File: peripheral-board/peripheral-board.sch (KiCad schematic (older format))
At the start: 7 parts, among them CON1001 AVR-ISP-10, IC1001 ATTINY48-A, P1001 Peripheral Bus, P1002 Power

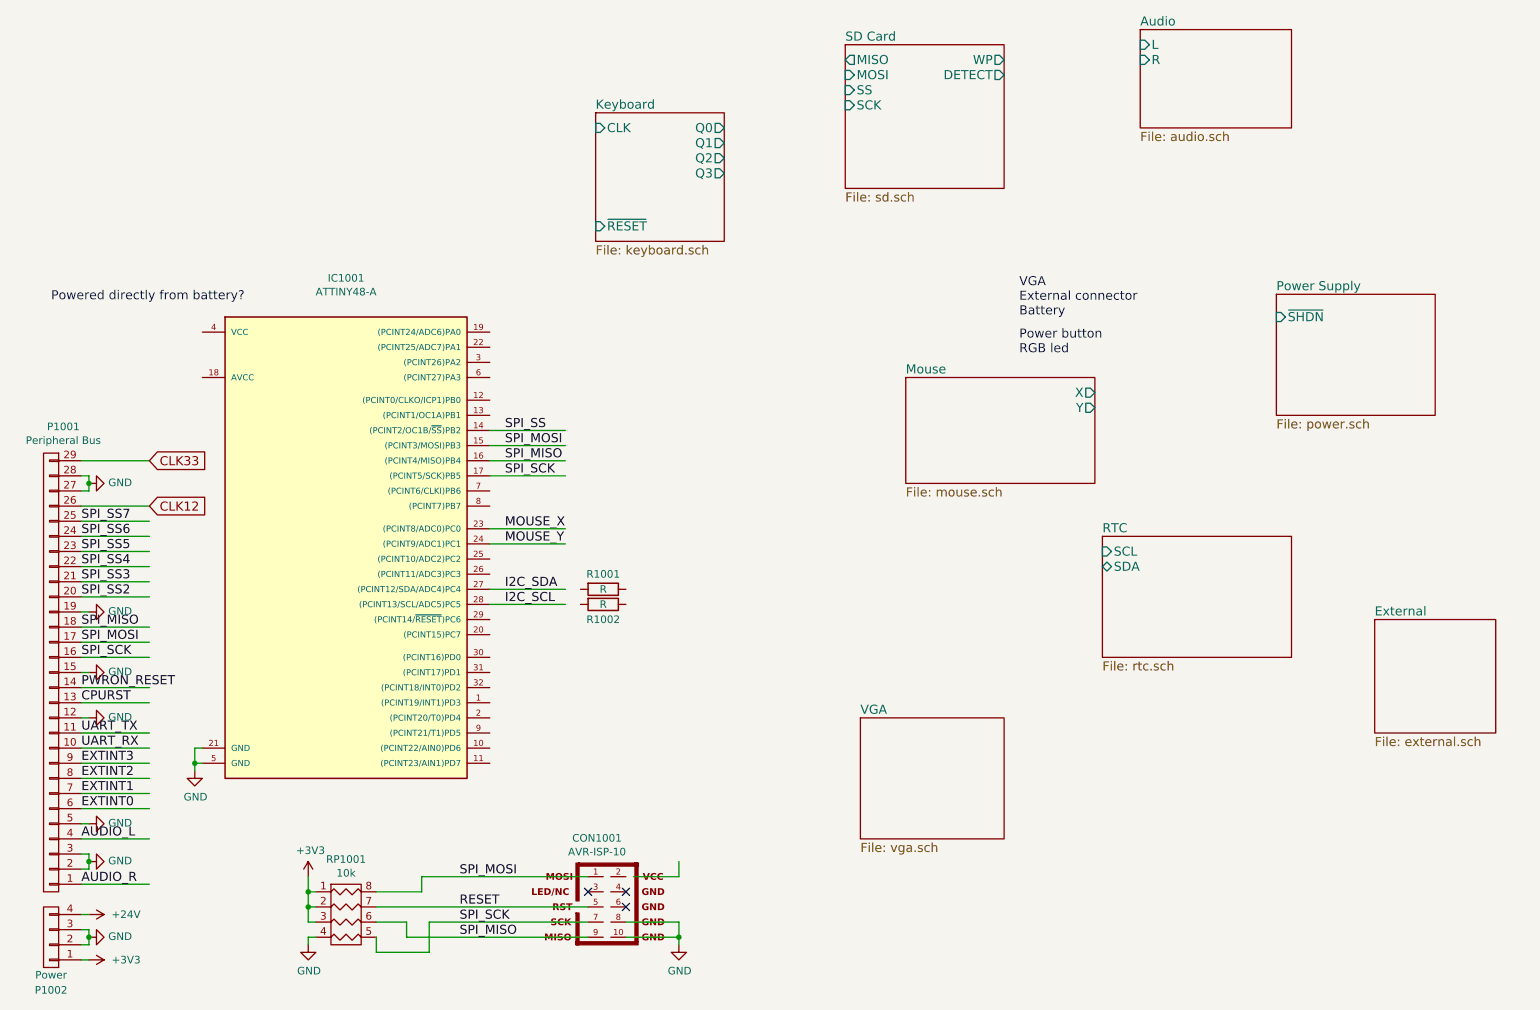
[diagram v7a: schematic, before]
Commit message: some more keyboard stuff fit on this side..
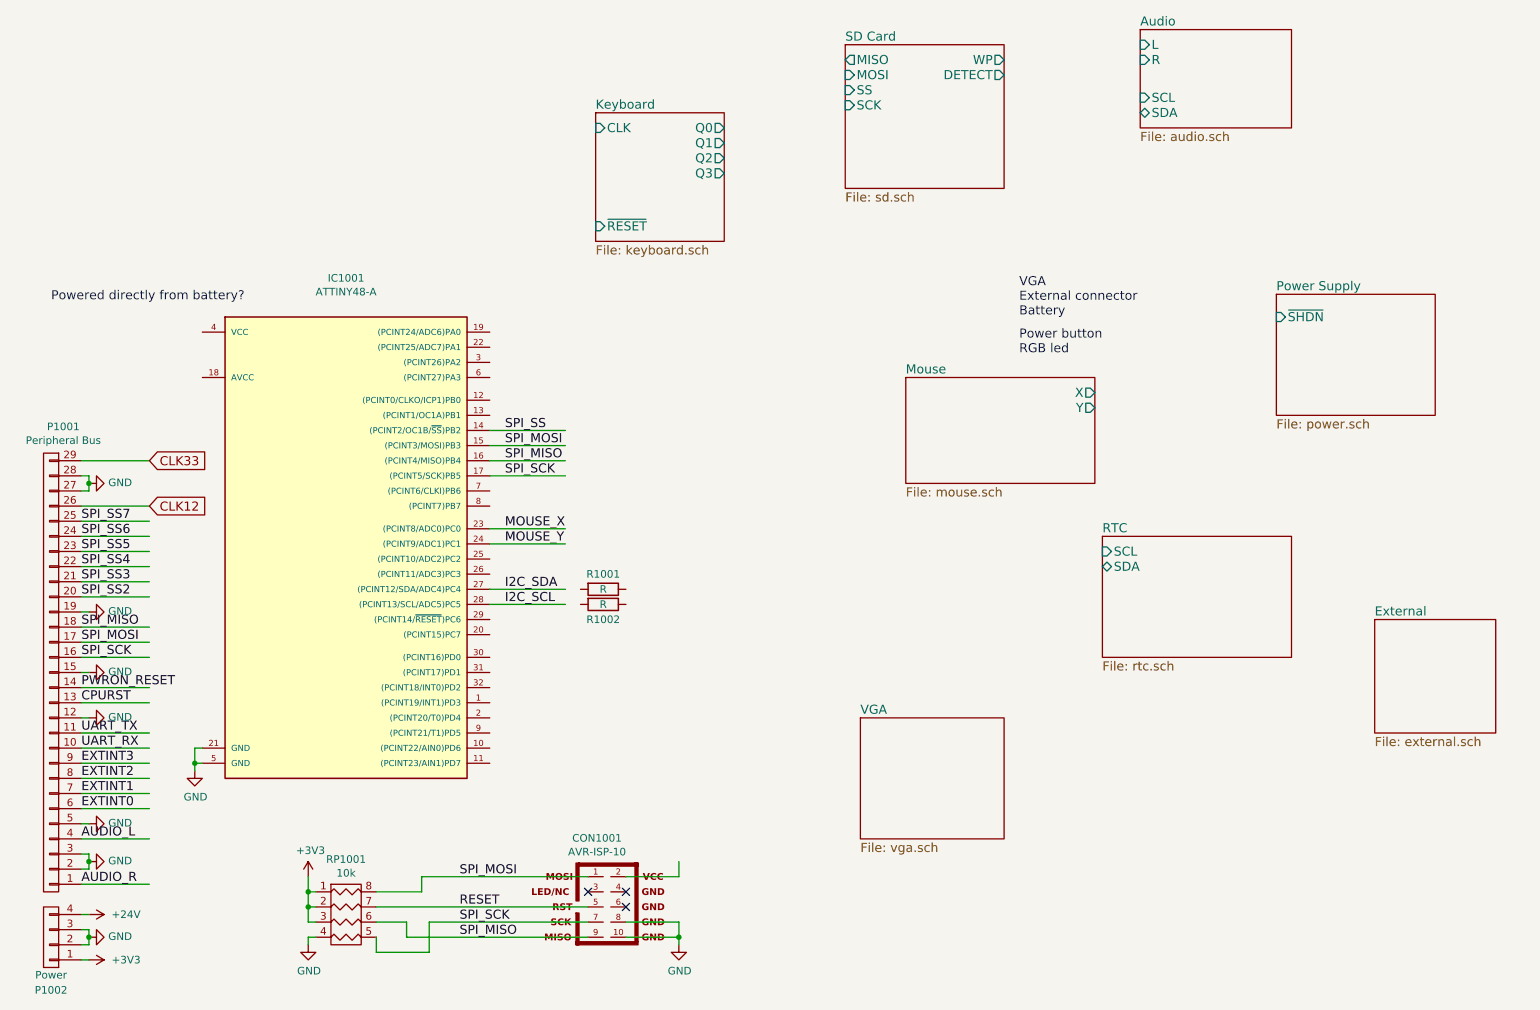
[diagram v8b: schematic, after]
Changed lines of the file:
@@
 F2 "L" I L 8200 900 60
 F3 "R" I L 8200 1000 60
+F4 "SDA" B L 8200 1350 60
+F5 "SCL" I L 8200 1250 60
 $EndSheet
 $Comp
@@
 	3350 6800 4550 6800
 Wire Wire Line
-	4850 6400 5150 6400
+	4800 6400 5150 6400
 Wire Wire Line
 	5150 6400 5150 6300
